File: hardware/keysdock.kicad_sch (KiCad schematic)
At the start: 0 parts

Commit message: :construction: new board
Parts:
- added C1, C10: 10uF, KeysDock:C_0402, symbol KeysDock:0402,10uF
- added C11, C14, C15, C16, C3, C9: 1uF, KeysDock:C_0402, symbol KeysDock:0402,1uF
- added C12, C8: 4.7uF, KeysDock:C_0402, symbol KeysDock:0402,4.7uF
- added C13, C5, C6, C7: 100nF, KeysDock:C_0402, symbol KeysDock:0402,100nF
- added C2: 3.3nF, KeysDock:C_0402, symbol KeysDock:0402,3.3nF
- added C4: 22uF, KeysDock:C_0402, symbol KeysDock:0402,22uF
- added D1: TPD1E10B06DPYR, KeysDock:DIO_TPD1E05U06DPYR, symbol components:TPD1E10B06DPYR
- added D2: SM4007PL, KeysDock:D_SOD-123FL, symbol KeysDock:SM4007PL
- added J1: TYPE-C 16PFS 2JCB1.2-H6.5 IPX8, KeysDock:USB-C-SMD_SHOUHAN_TYPE-C-16PFS-2JCB1.2-H6.5, symbol components:TYPE-C16PFS2JCB1.2-H6.5IPX8
- added L1: 2.2uH, KeysDock:IND-SMD_L2.5-W2.0_MHCHL2520, symbol KeysDock:FTC252012S2R2MBCA
- added PC1: HC-1.25-4PWT, KeysDock:HC-1.25-4PWT, symbol KeysDock:HC-1.25-4PWT
- added PC2: HC-1.25-2PWT, KeysDock:HC-1.25-2PWT, symbol KeysDock:HC-1.25-2PWT
- added R1, R11: 100Ω, KeysDock:R_0402, symbol KeysDock:0402,100Ω
- added R10, R12, R16, R2, R3, R9: 10kΩ, KeysDock:R_0402, symbol KeysDock:0402,10kΩ
- added R13: 1.10kΩ, KeysDock:R_0402, symbol KeysDock:0402,1.10kΩ
- added R14: 47kΩ, KeysDock:R_0402, symbol KeysDock:0402,47kΩ
- added R15: 750Ω, KeysDock:R_0402, symbol KeysDock:0402,750Ω
- added R17: 3kΩ, KeysDock:R_0402, symbol KeysDock:0402,3kΩ
- added R18, R19: 1.5kΩ, KeysDock:R_0402, symbol KeysDock:0402,1.5kΩ
- added R20, R21, R5: 100kΩ, KeysDock:R_0402, symbol KeysDock:0402,100kΩ
- added R4, R6: 22Ω, KeysDock:R_0402, symbol components:0402,22Ω
- added R7, R8: 5.1kΩ, KeysDock:R_0402, symbol components:0402,5.1kΩ
- added S1: TS24CA, KeysDock:TS24CA, symbol KeysDock:TS24CA
- added S2: TS-1088-AR02016, 160gf, KeysDock:SW_TS-1088-AR02016, symbol KeysDock:Tactile Button, 160gf, 12V, 50mA, 4.0mm
- added S3: SSSS811101, KeysDock:SW-SMD_SSSS811101, symbol KeysDock:SSSS811101
- added U1: TPD4E05U06DQAR, KeysDock:IC_TPD4E05U06DQAR, symbol components:TPD4E05U06DQAR
- added U2: TPS62142RGTR, KeysDock:QFN50P300X300X80-17N, symbol KeysDock:TPS62142RGTR
- added U3: ESP32-C6-WROOM-1-N8, KeysDock:ESP32-C6-WROOM-1, symbol KeysDock:ESP32-C6-WROOM-1
- added U4: BQ24074RGTR, KeysDock:QFN50P300X300X80-17N, symbol KeysDock:BQ24074RGTR
- added U5: TPS22910AYZVR, KeysDock:BGA4N50P2X2_88X88X50N, symbol KeysDock:TPS22910AYZVR
- added U6: TLA2518IRTER, KeysDock:QFN50P300X300X80-17N, symbol KeysDock:TLA2518IRTER
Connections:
- new net: R1.1, S1.1 (A)
- new net: J1.A6 (DP1), J1.B6 (DP2), R4.1, U1.10 (NC_10), U1.2 (D1-), U1.9 (NC_9)
- new net: R12.2, U4.1 (TS)
- new net: R13.2, U4.12 (ILIM)
- new net: R14.2, U4.14 (TMR)
- new net: R17.1, U4.15 (ITERM)
- new net: R15.2, U4.16 (ISET)
- new net: R16.2, U4.6 (EN1)
- new net: C3.1, R2.2, S1.2 (B), U3.3 (EN/CHIP_PU)
- new net: C15.1, U6.8 (DECAP)
- new net: R11.1, S2.2 (B)
- new net: J1.B5 (CC2), R7.1, U1.5 (D2-)
- new net: R5.1, U2.4 (PG)
- new net: J1.A5 (CC1), R8.1, U1.1 (D1+)
- new net: C13.1, R20.2, R21.2, U6.6 (AIN7/GPIO7)
- new net: L1.1, U2.1 (SW_1), U2.2 (SW_2), U2.3 (SW_3)
- new net: D2.1 (K), PC2.2, S3.1 (OUT1)
- new net: D2.2 (A), S3.3 (OUT2)
- new net: J1.A7 (DN1), J1.B7 (DN2), R6.1, U1.4 (D2+), U1.6 (NC_6), U1.7 (NC_7)
- new net: C2.1, U2.9 (SS/TR)
- new net BOOT_0: R10.2, S2.1 (A), U3.15 (GPIO9)
- new net BOOT_1: R9.2, U3.10 (GPIO8)
- new net GND: C1.2, C10.2, C11.2, C12.2, C16.2, C3.2, C4.2, C8.2, C9.2, D1.2, J1.B12A1 (GND), J1.B1A12 (GND), PC1.1, R1.2, R11.2, R12.1, R13.1, R14.1, R15.1, R17.2, R7.2, R8.2, U1.3 (GND), U1.8 (GND), U2.15 (PGND_15), U2.16 (PGND_16), U2.17 (EXP), U2.5 (FB), U2.7 (FSW), U2.8 (DEF), U3.1 (GND), U3.28 (GND), U3.29 (GND), U4.17 (EXP), U4.4 (~{CE}), U4.5 (EN2), U4.8 (VSS), U5.B1 (GND), U6.15 (AIN0/GPIO0), U6.16 (AIN1/GPIO1), U6.17 (GND), U6.9 (GND)
- new net KEYS_ADC_1: U6.1 (AIN2/GPIO2)
- new net KEYS_ADC_2: U6.2 (AIN3/GPIO3)
- new net KEYS_ADC_3: U6.3 (AIN4/GPIO4)
- new net KEYS_ADC_4: U6.4 (AIN5/GPIO5)
- new net KEYS_ADC_5: U6.5 (AIN6/GPIO6)
- new net KEYS_CH_A: U3.11 (GPIO10)
- new net KEYS_CH_B: U3.12 (GPIO11)
- new net KEYS_CH_C: U3.16 (GPIO18)
- new net KEYS_CH_CE: U3.21 (GPIO23)
- new net KEYS_CH_D: U3.17 (GPIO19)
- new net P,+: C1.1, C10.1, C12.1, U2.10 (AVIN), U2.11 (PVIN_11), U2.12 (PVIN_12), U2.13 (EN), U4.10 (OUT_10), U4.11 (OUT_11), U5.A2 (VIN)
- new net P,+3.3: C14.1, C16.1, C4.1, C5.1, C6.1, C7.1, L1.2, R10.1, R18.1, R19.1, R2.1, R3.1, R5.2, R9.1, U2.14 (VOS), U3.2 (3V3), U6.10 (DVDD), U6.7 (AVDD)
- new net P,E: C5.2, C6.2, C7.2, PC2.1, S3.4 (GND), S3.5 (GND), S3.6 (GND), S3.7 (GND)
- new net P,GND: C13.2, C14.2, C15.2, C2.2, R21.1, U2.6 (AGND)
- new net RANA: U3.18 (GPIO20)
- new net SAKI_MOVE: R3.2, U3.26 (GPIO3/ADC1_CH3)
- new net SPI_CLK: U3.6 (MTCK/GPIO6/ADC1_CH6), U6.13 (SCLK)
- new net SPI_CS_ADC: U3.20 (GPIO22), U6.11 (*CS)
- new net SPI_MISO: U3.27 (GPIO2/ADC1_CH2), U6.12 (SDO)
- new net SPI_MOSI: U3.7 (MTDO/GPIO7), U6.14 (SDI)
- new net TOMO0: U3.19 (GPIO21)
- new net U0RX: PC1.2, U3.24 (U0RXD/GPIO17)
- new net U0TX: PC1.3, U3.25 (U0TXD/GPIO16)
- new net USB_D+: R4.2, U3.14 (GPIO13/USB_D+)
- new net USB_D-: R6.2, U3.13 (GPIO12/USB_D-)
- new net VBAT: C8.1, R20.1, S3.2 (IN), U4.2 (BAT_2), U4.3 (BAT_3)
- new net VLED: C11.1, U5.A1 (VOUT)
- new net VUSB: C9.1, D1.1, J1.A4B9 (VBUS), J1.A9B4 (VBUS), PC1.4, R16.1, U4.13 (IN)
- new net ~{ANON}: U3.9 (GPIO1/ADC1_CH1/XTAL_32K_N), U5.B2 (ON)
- new net ~{BAT_CHG}: R18.2, U3.5 (MTDI/GPIO5/ADC1_CH5), U4.9 (~{CHG})
- new net ~{BAT_PGOOD}: R19.2, U3.4 (MTMS/GPIO4/ADC1_CH4), U4.7 (~{PGOOD})
- no-connect marks 0 -> 4
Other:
- added sheet keysgroup-1 (keysgroup.kicad_sch)
- added sheet keysgroup-2 (keysgroup.kicad_sch)
- added sheet keysgroup-3 (keysgroup.kicad_sch)
- added sheet keysgroup-4 (keysgroup.kicad_sch)
- added sheet keysgroup-5 (keysgroup-last.kicad_sch)
- added sheet leds (leds.kicad_sch)
- note added: "Pin Definitions ~{ANON}: LED enable pin, low is active. TOMO0: LED WS2812 data pin. RANA: Sleep control pin; active low for the working state, and active high for the sleep state. KEYS_CH_*: Multiplexer switching pins. KEYS_ADC_OUT: Button group sampling output. SAKI_MOVE: Sleep wake-up pin; outputs a low signal when a button pressed during the sleep state. Note: ~{ANON} comes from Chihaya Anon (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"
- title: KeysDock PCB -> KeysDock Panel

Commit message: :construction: some chip layout
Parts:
- D1: symbol components:TPD1E10B06DPYR -> KeysDock:TPD1E10B06DPYR
- J1: symbol components:TYPE-C16PFS2JCB1.2-H6.5IPX8 -> KeysDock:TYPE-C16PFS2JCB1.2-H6.5IPX8
- R4, R6: symbol components:0402,22Ω -> KeysDock:0402,22Ω
- R7, R8: symbol components:0402,5.1kΩ -> KeysDock:0402,5.1kΩ
- U1: symbol components:TPD4E05U06DQAR -> KeysDock:TPD4E05U06DQAR
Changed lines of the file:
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@@
 	)
 	(symbol
-		(lib_id "components:0402,22Ω")
+		(lib_id "KeysDock:0402,22Ω")
 		(at 86.36 251.46 0)
 		(unit 1)
@@
 	)
 	(symbol
-		(lib_id "components:0402,5.1kΩ")
+		(lib_id "KeysDock:0402,5.1kΩ")
 		(at 96.52 251.46 0)
 		(unit 1)
@@
 	)
 	(symbol
-		(lib_id "components:0402,5.1kΩ")
+		(lib_id "KeysDock:0402,5.1kΩ")
 		(at 99.06 251.46 0)
 		(unit 1)
@@
 	)
 	(symbol
-		(lib_id "components:TPD4E05U06DQAR")
+		(lib_id "KeysDock:TPD4E05U06DQAR")
 		(at 54.61 246.38 0)
 		(mirror y)
@@
 	)
 	(symbol
-		(lib_id "components:TYPE-C16PFS2JCB1.2-H6.5IPX8")
+		(lib_id "KeysDock:TYPE-C16PFS2JCB1.2-H6.5IPX8")
 		(at 87.63 210.82 270)
 		(mirror x)
@@
 	)
 	(symbol
-		(lib_id "components:TPD1E10B06DPYR")
+		(lib_id "KeysDock:TPD1E10B06DPYR")
 		(at 115.57 231.14 0)
 		(unit 1)
@@
 	)
 	(symbol
-		(lib_id "components:0402,22Ω")
+		(lib_id "KeysDock:0402,22Ω")
 		(at 88.9 251.46 0)
 		(unit 1)

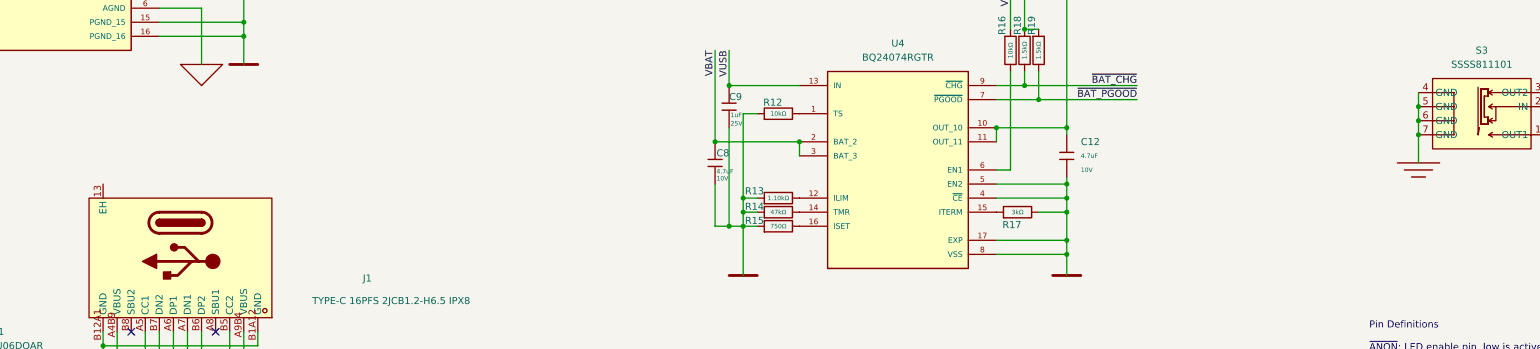
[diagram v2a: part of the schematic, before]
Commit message: :construction: awake and sleep lines
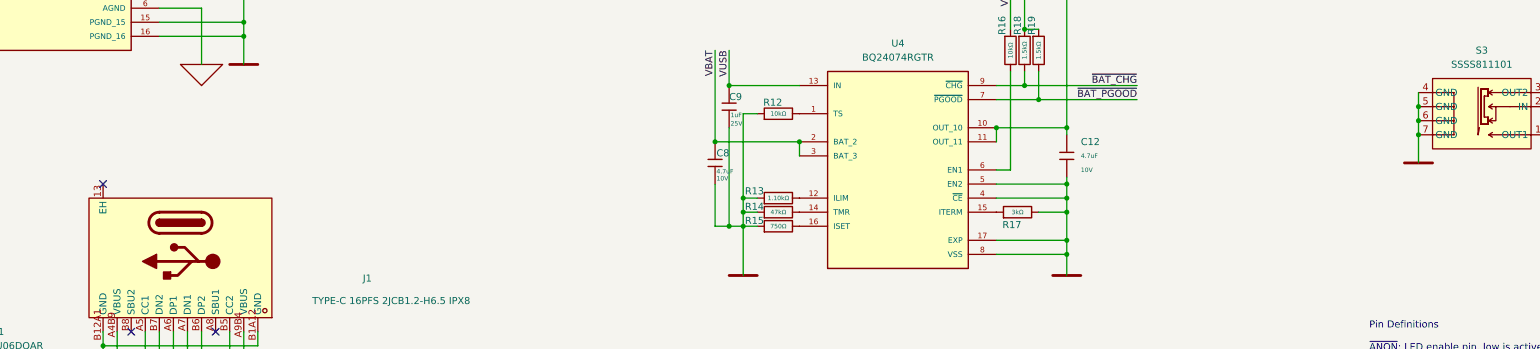
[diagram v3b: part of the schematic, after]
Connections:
- net GND: now also S3.4 (GND), S3.5 (GND), S3.6 (GND), S3.7 (GND)
- net P,E: no longer S3.4 (GND), S3.5 (GND), S3.6 (GND), S3.7 (GND)
- no-connect marks 4 -> 5
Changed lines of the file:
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@@
 	)
 	(no_connect
+		(at 73.66 191.77)
+	)
+	(no_connect
 		(at 78.74 218.44)
 	)
@@
 	(symbol
 		(lib_id "PCM_Generic:P,0")
+		(at 311.15 187.96 0)
+		(unit 1)
+		(body_style 1)
+		(exclude_from_sim no)
+		(in_bom yes)
+		(on_board yes)
+		(in_pos_files yes)
+		(dnp no)
+		(fields_autoplaced yes)
+		(property "Reference" "#PWR031"
+			(at 314.96 184.15 0)
+			(hide yes)
+			(show_name no)
+			(do_not_autoplace no)
+			(effects
+				(font
+					(size 2.54 2.54)
+				)
+				(justify left)
+			)
+		)
+		(property "Value" "P,0"
+			(at 314.96 187.96 0)
+			(hide yes)
+			(show_name no)
+			(do_not_autoplace no)
+			(effects
+				(font
+					(size 0.001 0.001)
+				)
+				(justify left)
+			)
+		)
+		(property "Footprint" ""
+			(at 311.15 187.96 0)
+			(hide yes)
+			(show_name no)
+			(do_not_autoplace no)
+			(effects
+				(font
+					(size 2.54 2.54)
+				)
+			)
+		)
+		(property "Datasheet" ""
+			(at 311.15 187.96 0)
+			(hide yes)
+			(show_name no)
+			(do_not_autoplace no)
+			(effects
+				(font
+					(size 2.54 2.54)
+				)
+			)
+		)
+		(property "Description" "global node 0; simplified functional (equipotential) bonding (FB); simplified frame/chassis"
+			(at 311.15 187.96 0)
+			(hide yes)
+			(show_name no)
+			(do_not_autoplace no)
+			(effects
+				(font
+					(size 1.27 1.27)
+				)
+			)
+		)
+		(pin "0"
+		)
+		(instances
+			(project "keysdock"
+				(path "/1dbf2a4e-9b9b-4b09-9979-c8b99f6b5d2a"
+					(reference "#PWR031")
+					(unit 1)
+				)
+			)
+		)
+	)
+	(symbol
+		(lib_id "PCM_Generic:P,0")
 		(at 73.66 226.06 0)
 		(unit 1)
@@
 					(unit 1)
 				)
-			)
-		)
-	)
-	(symbol
-		(lib_id "PCM_Generic:P,E")
-		(at 311.15 187.96 0)
-		(unit 1)
-		(body_style 1)
-		(exclude_from_sim no)
-		(in_bom yes)
-		(on_board yes)
-		(in_pos_files yes)
-		(dnp no)
-		(fields_autoplaced yes)
-		(property "Reference" "#PWR031"
-			(at 314.96 184.15 0)
-			(hide yes)
-			(show_name no)
-			(do_not_autoplace no)
-			(effects
-				(font
-					(size 2.54 2.54)
-				)
-				(justify left)
-			)
-		)
-		(property "Value" "P,E"
-			(at 314.96 187.96 0)
-			(hide yes)
-			(show_name no)
-			(do_not_autoplace no)
-			(effects
-				(font
-					(size 0.001 0.001)
-				)
-				(justify left)
-			)
-		)
-		(property "Footprint" ""
-			(at 311.15 187.96 0)
-			(hide yes)
-			(show_name no)
-			(do_not_autoplace no)
-			(effects
-				(font
-					(size 2.54 2.54)
-				)
-			)
-		)
-		(property "Datasheet" ""
-			(at 311.15 187.96 0)
-			(hide yes)
-			(show_name no)
-			(do_not_autoplace no)
-			(effects
-				(font
-					(size 2.54 2.54)
-				)
-			)
-		)
-		(property "Description" "earth/ground/earthing/grounding (E)"
-			(at 311.15 187.96 0)
-			(hide yes)
-			(show_name no)
-			(do_not_autoplace no)
-			(effects
-				(font
-					(size 1.27 1.27)
-				)
-			)
-		)
-		(pin "0"
-		)
-		(instances
-			(project "keysdock"
-				(path "/1dbf2a4e-9b9b-4b09-9979-c8b99f6b5d2a"
-					(reference "#PWR031")
-					(unit 1)
-				)

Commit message: :construction: lines for controller
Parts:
- added R24: 0Ω, KeysDock:R_0402, symbol KeysDock:0402,0Ω
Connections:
- net P,E is gone; now on net GND: C5.2, C6.2, C7.2, PC2.1
- net GND: now also R24.1
- net P,GND: now also R24.2

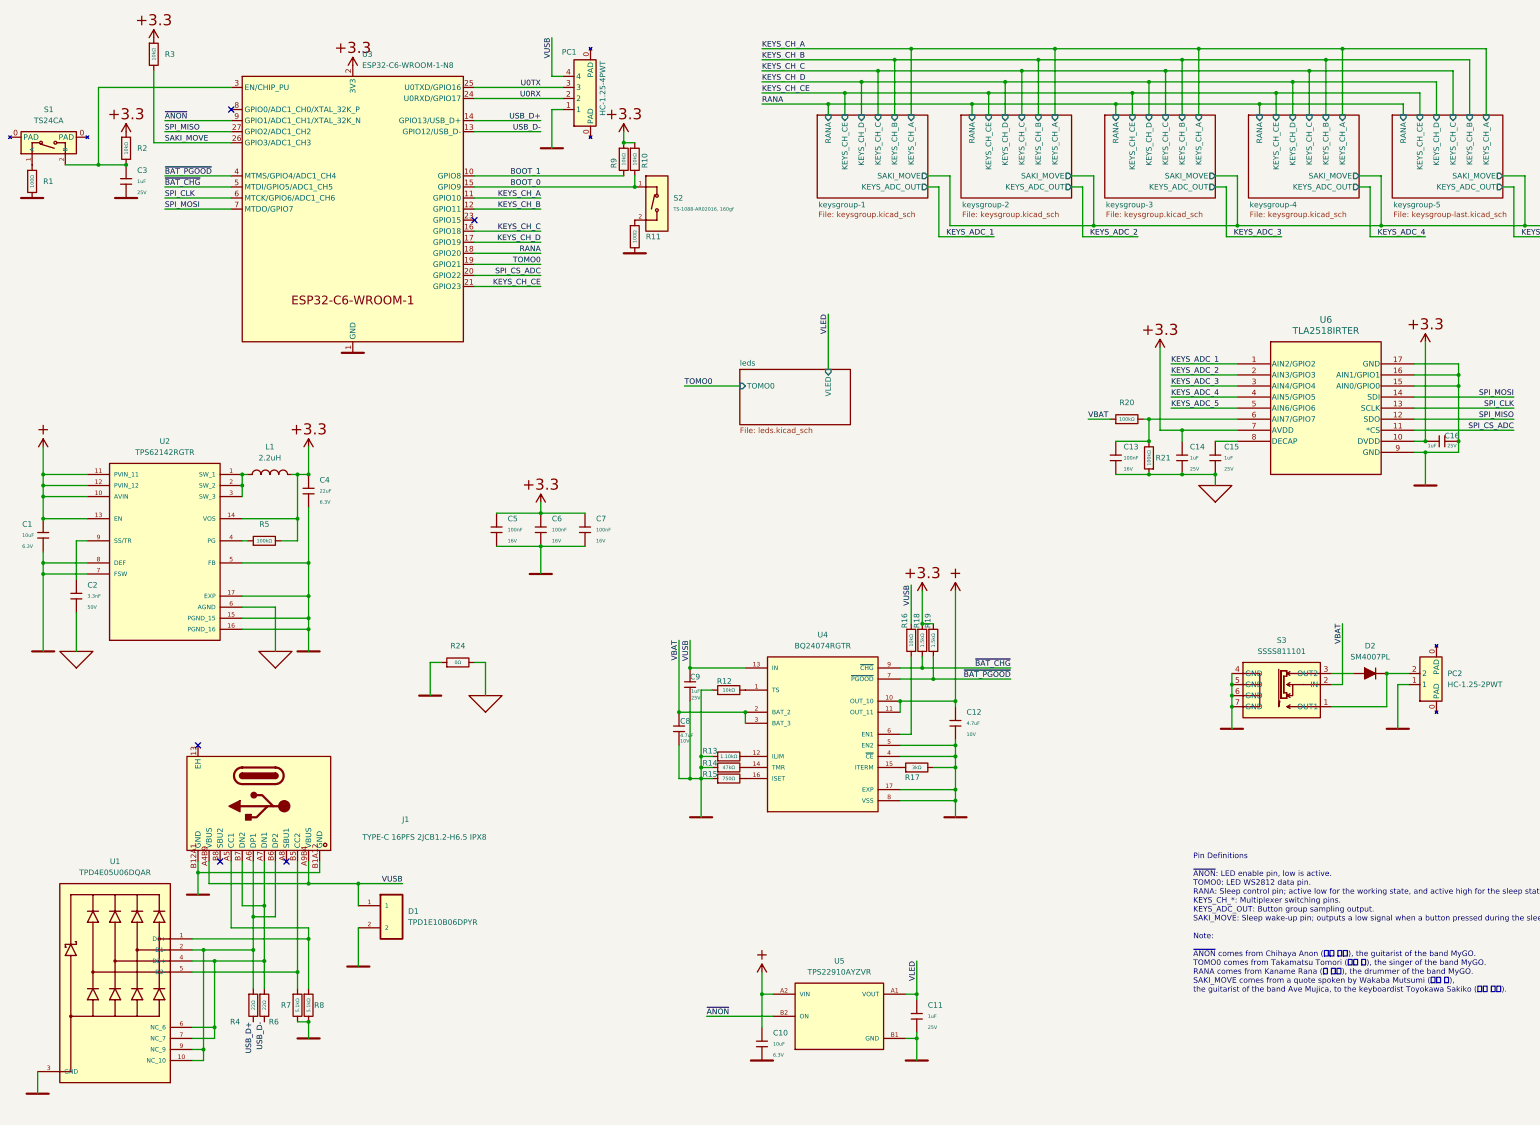
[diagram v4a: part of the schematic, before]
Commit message: :sparkles: use net tie to construct GNDs
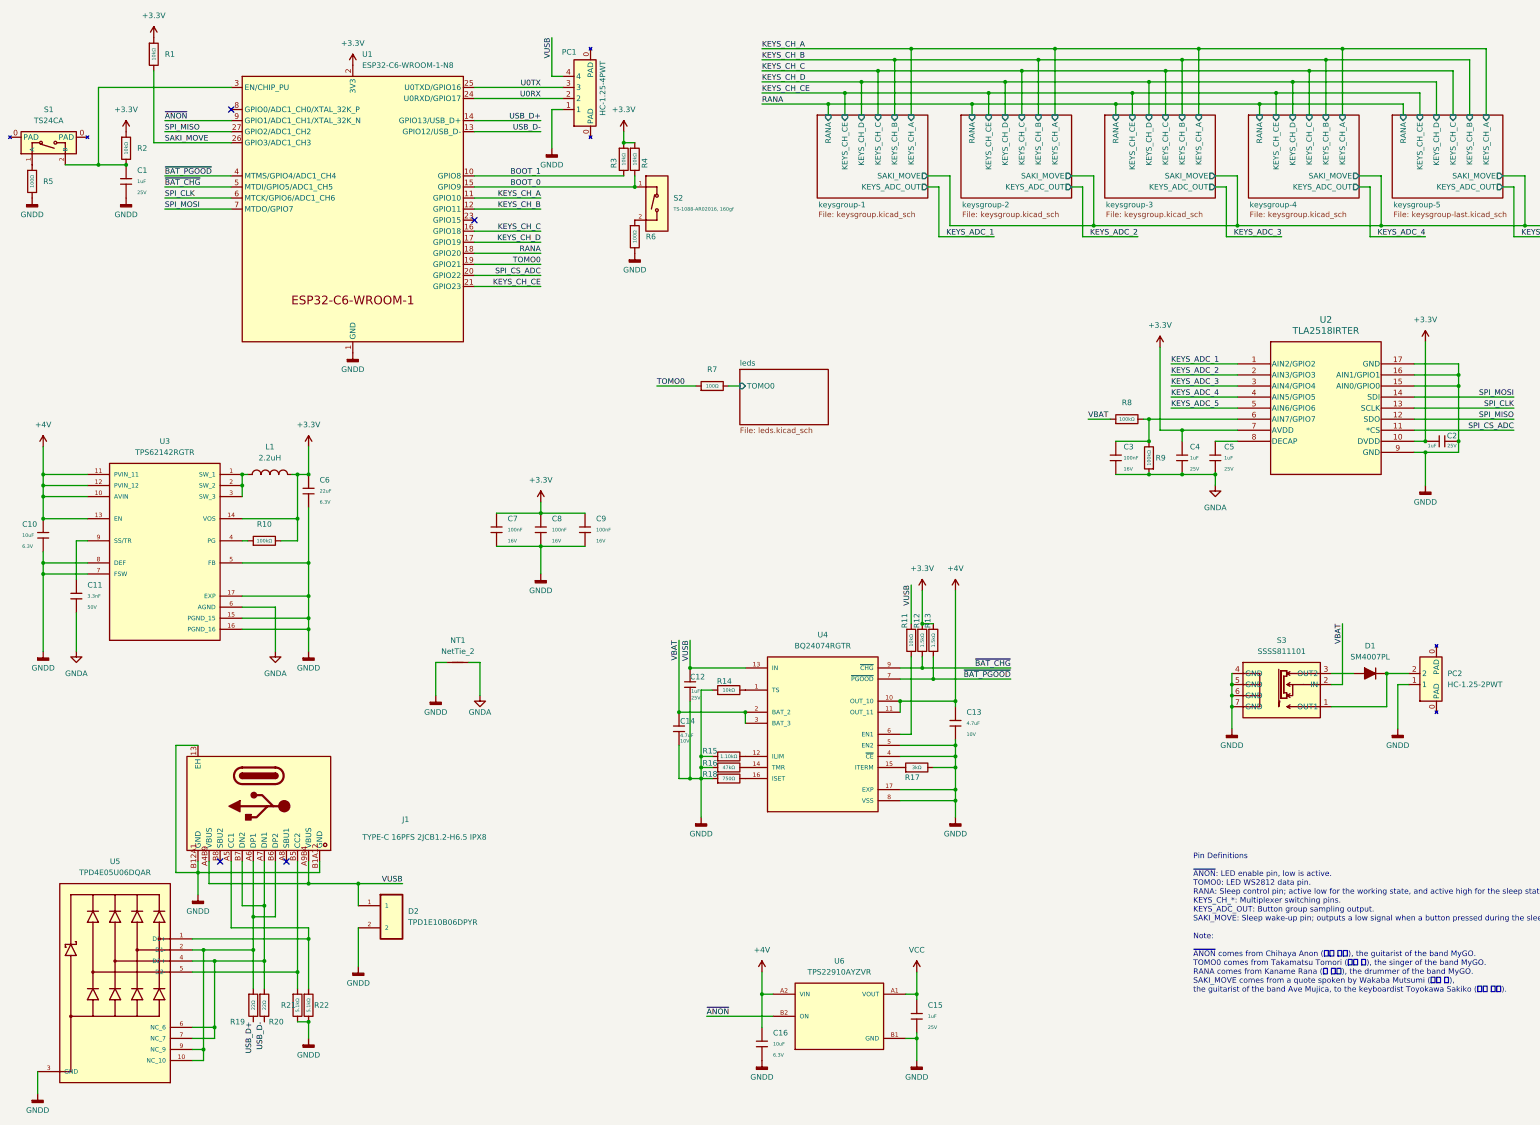
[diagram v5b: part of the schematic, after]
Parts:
- removed R24: 0Ω, KeysDock:R_0402, symbol KeysDock:0402,0Ω
- added NT1: NetTie_2, NetTie:NetTie-2_THT_Pad1.0mm, symbol Device:NetTie_2
- added R7: 100Ω, KeysDock:R_0402, symbol KeysDock:0402,100Ω
- renumbered C3 to C1, C1 to C10, C2 to C11, C9 to C12, C12 to C13, C8 to C14, C11 to C15, C10 to C16, C16 to C2, C13 to C3, C14 to C4, C15 to C5, C4 to C6, C5 to C7, C6 to C8, C7 to C9, D2 to D1, D1 to D2, R3 to R1, R5 to R10, R16 to R11, R18 to R12, R19 to R13, R12 to R14, R13 to R15, R14 to R16, R15 to R18, R4 to R19, R6 to R20, R7 to R21, R8 to R22, R9 to R3, R10 to R4, R1 to R5, R11 to R6, R20 to R8, R21 to R9, U3 to U1, U6 to U2, U2 to U3, U1 to U5, U5 to U6
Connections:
- net GND: now also J1.13 (EH), NT1.1
- net TOMO0: now also R7.1
- net P,+ renamed +4V
- net P,+3.3 renamed +3.3V
- net P,GND renamed GNDA
- net GNDA: now also NT1.2
- net VLED renamed VCC
- new net leds/TOMO0: R7.2
- no-connect marks 5 -> 4
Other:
- sheet leds ports: added none; removed VLED
